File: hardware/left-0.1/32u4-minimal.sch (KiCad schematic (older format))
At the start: 15 parts, among them SW35 SW_Push, U2 ATmega32U4-AU, Y1 16MHz

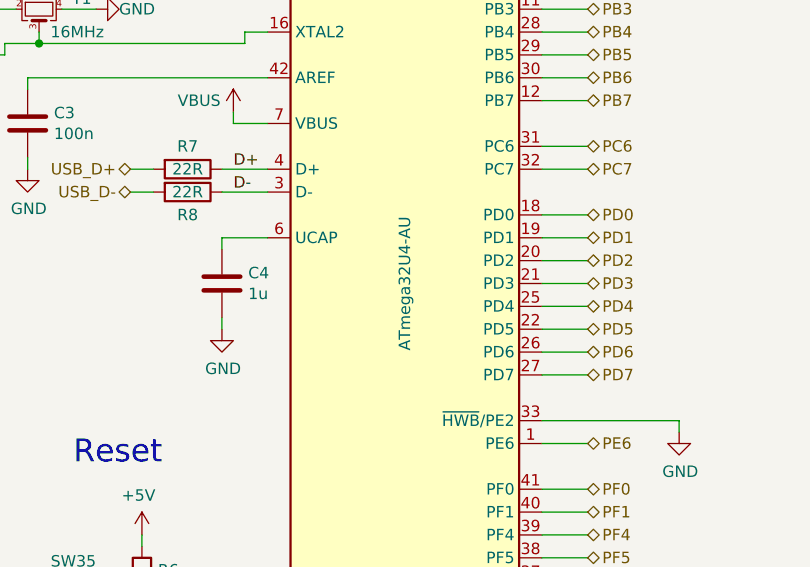
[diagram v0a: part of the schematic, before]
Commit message: first go at board outline done
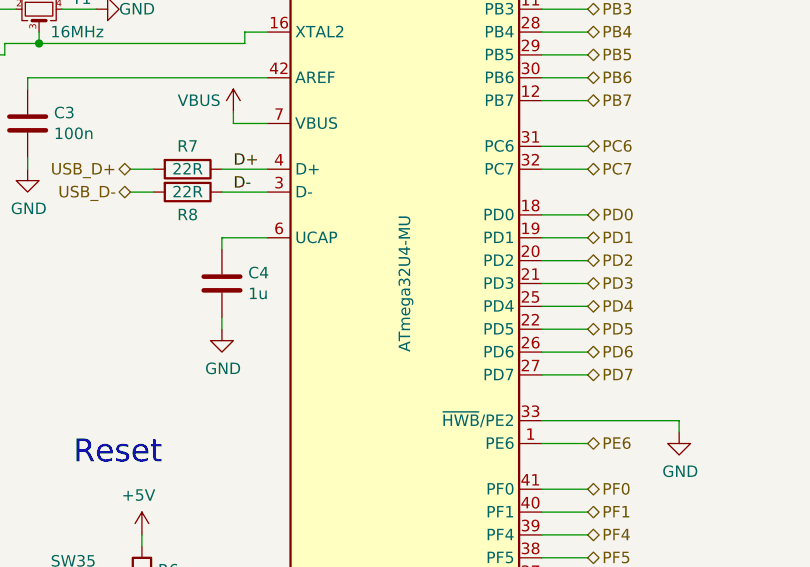
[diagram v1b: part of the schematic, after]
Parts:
- removed U2: ATmega32U4-AU, Package_QFP:TQFP-44_10x10mm_P0.8mm, symbol MCU_Microchip_ATmega:ATmega32U4-AU
- added U2: ATmega32U4-MU, Package_DFN_QFN:QFN-44-1EP_7x7mm_P0.5mm_EP5.2x5.2mm, symbol MCU_Microchip_ATmega:ATmega32U4-MU
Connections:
- net +5V: now also U2.14 (VCC), U2.24 (AVCC), U2.34 (VCC), U2.44 (AVCC)
- net D+: now also U2.4 (D+)
- net D-: now also U2.3 (D-)
- net GND: now also U2.15 (GND), U2.23 (GND), U2.33 (~HWB~/PE2), U2.35 (GND), U2.43 (GND), U2.45 (GND), U2.5 (UGND)
- net PB0: now also U2.8 (PB0)
- net PB1: now also U2.9 (PB1)
- net PB2: now also U2.10 (PB2)
- net PB3: now also U2.11 (PB3)
- net PB4: now also U2.28 (PB4)
- net PB5: now also U2.29 (PB5)
- net PB6: now also U2.30 (PB6)
- net PB7: now also U2.12 (PB7)
- net PC6: now also U2.31 (PC6)
- net PC7: now also U2.32 (PC7)
- net PD0: now also U2.18 (PD0)
- net PD1: now also U2.19 (PD1)
- net PD2: now also U2.20 (PD2)
- net PD3: now also U2.21 (PD3)
- net PD4: now also U2.25 (PD4)
- net PD5: now also U2.22 (PD5)
- net PD6: now also U2.26 (PD6)
- net PD7: now also U2.27 (PD7)
- net PE6: now also U2.1 (PE6)
- net PF0: now also U2.41 (PF0)
- net PF1: now also U2.40 (PF1)
- net PF4: now also U2.39 (PF4)
- net PF5: now also U2.38 (PF5)
- net PF6: now also U2.37 (PF6)
- net PF7: now also U2.36 (PF7)
- net VBUS: now also U2.2 (UVCC), U2.7 (VBUS)
- net nRST: now also U2.13 (~RESET)
- net at C1.1, Y1.1: now also U2.17 (XTAL1)
- net at C2.1, Y1.3: now also U2.16 (XTAL2)
- net at C4.1: now also U2.6 (UCAP)
- net at C3.1: now also U2.42 (AREF)
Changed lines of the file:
@@
 PF7
 $Comp
-L MCU_Microchip_ATmega:ATmega32U4-AU U2
-U 1 1 5F4370D6
+L MCU_Microchip_ATmega:ATmega32U4-MU U2
+U 1 1 5E24D58F
 P 3900 4400
 F 0 "U2" H 3450 6150 50  0000 C CNN
-F 1 "ATmega32U4-AU" V 3900 4400 50  0000 C CNN
-F 2 "Package_QFP:TQFP-44_10x10mm_P0.8mm" H 3900 4400 50  0001 C CIN
+F 1 "ATmega32U4-MU" V 3900 4400 50  0000 C CNN
+F 2 "Package_DFN_QFN:QFN-44-1EP_7x7mm_P0.5mm_EP5.2x5.2mm" H 3900 4400 50  0001 C CIN
 F 3 "http://ww1.microchip.com/downloads/en/DeviceDoc/Atmel-7766-8-bit-AVR-ATmega16U4-32U4_Datasheet.pdf" H 3900 4400 50  0001 C CNN
-F 4 "ATMEGA32U4-AURCT-ND" H 3900 4400 50  0001 C CNN "Digikey"
-F 5 "C44854" H 3900 4400 50  0001 C CNN "LCSC"
-F 6 "ATMEGA32U4-AU" H 3900 4400 50  0001 C CNN "MPN"
 	1    3900 4400
 	1    0    0    -1

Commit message: left all connected
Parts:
- added J3: AVR-ISP-6, josh-connectors:AVR_Programmer_SMD, symbol Connector:AVR-ISP-6
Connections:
- net +5V: now also J3.2 (VCC)
- net GND: now also J3.6 (GND)
- net PB1: now also J3.3 (SCK)
- net PB2: now also J3.4 (MOSI)
- net PB3: now also J3.1 (MISO)
- net nRST: now also J3.5 (~RST)
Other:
- note added: "Programming Header"
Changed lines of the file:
@@
 $Descr A4 11693 8268
 encoding utf-8
-Sheet 2 2
+Sheet 2 3
 Title ""
 Date ""
@@
 $Comp
 L MCU_Microchip_ATmega:ATmega32U4-MU U2
-U 1 1 5E24D58F
+U 1 1 5FB07BE0
 P 3900 4400
 F 0 "U2" H 3450 6150 50  0000 C CNN
@@
 	1    0    0    -1
 $EndComp
+$Comp
+L Connector:AVR-ISP-6 J3
+U 1 1 5E3F772B
+P 6450 5550
+F 0 "J3" H 6200 6000 50  0000 R CNN
+F 1 "AVR-ISP-6" H 6800 6000 50  0000 R CNN
+F 2 "josh-connectors:AVR_Programmer_SMD" V 6200 5600 50  0001 C CNN
+F 3 " ~" H 5175 5000 50  0001 C CNN
+	1    6450 5550
+	1    0    0    -1
+$EndComp
+Wire Wire Line
+	6350 5950 6350 6000
+$Comp
+L power:GND #PWR0209
+U 1 1 5E3FABE7
+P 6350 6000
+F 0 "#PWR0209" H 6350 5750 50  0001 C CNN
+F 1 "GND" H 6355 5827 50  0000 C CNN
+F 2 "" H 6350 6000 50  0001 C CNN
+F 3 "" H 6350 6000 50  0001 C CNN
+	1    6350 6000
+	1    0    0    -1
+$EndComp
+Wire Wire Line
+	6350 5050 6350 5000
+$Comp
+L power:+5V #PWR0210
+U 1 1 5E3FD90D
+P 6350 5000
+F 0 "#PWR0210" H 6350 4850 50  0001 C CNN
+F 1 "+5V" H 6365 5173 50  0000 C CNN
+F 2 "" H 6350 5000 50  0001 C CNN
+F 3 "" H 6350 5000 50  0001 C CNN
+	1    6350 5000
+	1    0    0    -1
+$EndComp
+Text Label 7150 5650 2    50   ~ 0
+nRST
+Wire Wire Line
+	7150 5650 6850 5650
+Text Notes 5800 4700 0    100  ~ 0
+Programming Header
+Text HLabel 7150 5350 2    50   BiDi ~ 0
+PB3
+Wire Wire Line
+	7150 5350 6850 5350
+Wire Wire Line
+	6850 5450 7150 5450
+Wire Wire Line
+	6850 5550 7150 5550
+Text HLabel 7150 5550 2    50   BiDi ~ 0
+PB1
+Text HLabel 7150 5450 2    50   BiDi ~ 0
+PB2
 $EndSCHEMATC

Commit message: layout looking nice, just graphics to go
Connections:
- no-connect marks 0 -> 3
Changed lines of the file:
@@
 Wire Wire Line
 	3300 4000 3100 4000
-$Comp
-L power:PWR_FLAG #FLG0104
-U 1 1 5E724506
-P 6850 7500
-F 0 "#FLG0104" H 6850 7575 50  0001 C CNN
-F 1 "PWR_FLAG" V 6850 7800 50  0000 C CNN
-F 2 "" H 6850 7500 50  0001 C CNN
-F 3 "~" H 6850 7500 50  0001 C CNN
-	1    6850 7500
-	1    0    0    -1
-$EndComp
-$Comp
-L power:GND #PWR0192
-U 1 1 5E727AD7
-P 6850 7550
-F 0 "#PWR0192" H 6850 7300 50  0001 C CNN
-F 1 "GND" H 6855 7377 50  0000 C CNN
-F 2 "" H 6850 7550 50  0001 C CNN
-F 3 "" H 6850 7550 50  0001 C CNN
-	1    6850 7550
-	1    0    0    -1
-$EndComp
-Wire Wire Line
-	6850 7550 6850 7500
 Text Label 3150 3900 0    50   ~ 0
 D+
@@
 Text HLabel 7150 5450 2    50   BiDi ~ 0
 PB2
+NoConn ~ 4500 3300
+NoConn ~ 4500 2900
+NoConn ~ 4500 4800
 $EndSCHEMATC

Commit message: updated components due to jlk change
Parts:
- J3: footprint josh-connectors:AVR_Programmer_SMD -> josh-connectors:AVR_PROG_2.54_SMT
- SW35: footprint josh-buttons-switches:BT_Small_2_Pin -> josh-buttons-switches:SW_Push_PTS820
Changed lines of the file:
@@
 F 0 "SW35" H 2450 6185 50  0000 C CNN
 F 1 "SW_Push" H 2450 6094 50  0000 C CNN
-F 2 "josh-buttons-switches:BT_Small_2_Pin" H 2450 6100 50  0001 C CNN
+F 2 "josh-buttons-switches:SW_Push_PTS820" H 2450 6100 50  0001 C CNN
 F 3 "~" H 2450 6100 50  0001 C CNN
 F 4 "401-1704-1-ND" H 2450 5900 50  0001 C CNN "Digikey"
@@
 F 0 "J3" H 6200 6000 50  0000 R CNN
 F 1 "AVR-ISP-6" H 6800 6000 50  0000 R CNN
-F 2 "josh-connectors:AVR_Programmer_SMD" V 6200 5600 50  0001 C CNN
+F 2 "josh-connectors:AVR_PROG_2.54_SMT" V 6200 5600 50  0001 C CNN
 F 3 " ~" H 5175 5000 50  0001 C CNN
 	1    6450 5550

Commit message: more layout
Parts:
- C1, C2: DigiKey (none) -> 1276-2228-1-ND; Digikey 1276-2228-1-ND -> (none)
- C3, C6, C7: DigiKey (none) -> 1276-1000-1-ND; Digikey 1276-1000-1-ND -> (none)
- C4, C5: DigiKey (none) -> 1276-1866-1-ND; Digikey 1276-1866-1-ND -> (none)
- D36: DigiKey (none) -> 732-4980-1-ND; Digikey 732-4980-1-ND -> (none)
- R5: DigiKey (none) -> CR0603-JW-222ELFCT-ND; Digikey CR0603-JW-222ELFCT-ND -> (none)
- R6: DigiKey (none) -> CR0603-JW-103ELFCT-ND; Digikey CR0603-JW-103ELFCT-ND -> (none)
- R7, R8: DigiKey (none) -> CR0603-JW-220ELFCT-ND; Digikey CR0603-JW-220ELFCT-ND -> (none)
- SW35: DigiKey (none) -> 401-1704-1-ND; Digikey 401-1704-1-ND -> (none)
- Y1: DigiKey (none) -> 535-9134-1-ND; Digikey 535-9134-1-ND -> (none)
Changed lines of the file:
@@
 F 2 "Capacitor_SMD:C_0603_1608Metric" H 4238 2100 50  0001 C CNN
 F 3 "~" H 4200 2250 50  0001 C CNN
-F 4 "1276-1000-1-ND" H 4200 2250 50  0001 C CNN "Digikey"
+F 4 "1276-1000-1-ND" H 4200 2250 50  0001 C CNN "DigiKey"
 F 5 "CL10B104KB8NNNC" H 4200 2250 50  0001 C CNN "MPN"
 	1    4200 2250
@@
 F 2 "Capacitor_SMD:C_0603_1608Metric" H 4238 1850 50  0001 C CNN
 F 3 "~" H 4200 2000 50  0001 C CNN
-F 4 "1276-1000-1-ND" H 4200 2000 50  0001 C CNN "Digikey"
+F 4 "1276-1000-1-ND" H 4200 2000 50  0001 C CNN "DigiKey"
 F 5 "CL10B104KB8NNNC" H 4200 2000 50  0001 C CNN "MPN"
 	1    4200 2000
@@
 F 2 "Capacitor_SMD:C_0603_1608Metric" H 4238 1600 50  0001 C CNN
 F 3 "~" H 4200 1750 50  0001 C CNN
-F 4 "1276-1866-1-ND " H 4200 1750 50  0001 C CNN "Digikey"
+F 4 "1276-1866-1-ND " H 4200 1750 50  0001 C CNN "DigiKey"
 F 5 "CL10A105MP8NNNC " H 4200 1750 50  0001 C CNN "MPN"
 	1    4200 1750
@@
 F 2 "Capacitor_SMD:C_0603_1608Metric" H 1988 2850 50  0001 C CNN
 F 3 "~" H 1950 3000 50  0001 C CNN
-F 4 "1276-2228-1-ND " H 1950 3000 50  0001 C CNN "Digikey"
+F 4 "1276-2228-1-ND " H 1950 3000 50  0001 C CNN "DigiKey"
 F 5 "CL10C220JB8NFNC " H 1950 3000 50  0001 C CNN "MPN"
 	1    1950 3000
@@
 F 2 "Capacitor_SMD:C_0603_1608Metric" H 1988 3250 50  0001 C CNN
 F 3 "~" H 1950 3400 50  0001 C CNN
-F 4 "1276-2228-1-ND " H 1950 3400 50  0001 C CNN "Digikey"
+F 4 "1276-2228-1-ND " H 1950 3400 50  0001 C CNN "DigiKey"
 F 5 "CL10C220JB8NFNC " H 1950 3400 50  0001 C CNN "MPN"
 	1    1950 3400
@@
 F 2 "josh-oscillators:Crystal_SMD_3225-4Pin_3.2x2.5mm" H 2300 3200 50  0001 C CNN
 F 3 "~" H 2300 3200 50  0001 C CNN
-F 4 "535-9134-1-ND" H 2300 3200 50  0001 C CNN "Digikey"
+F 4 "535-9134-1-ND" H 2300 3200 50  0001 C CNN "DigiKey"
 F 5 "C179641" H 2300 3200 50  0001 C CNN "LCSC"
 F 6 "ABM8-16.000MHZ-B2-T" H 2300 3200 50  0001 C CNN "MPN"
@@
 F 2 "Capacitor_SMD:C_0603_1608Metric" H 3138 4250 50  0001 C CNN
 F 3 "~" H 3100 4400 50  0001 C CNN
-F 4 "1276-1866-1-ND " H 3100 4400 50  0001 C CNN "Digikey"
+F 4 "1276-1866-1-ND " H 3100 4400 50  0001 C CNN "DigiKey"
 F 5 "CL10A105MP8NNNC " H 3100 4400 50  0001 C CNN "MPN"
 	1    3100 4400
@@
 F 2 "Capacitor_SMD:C_0603_1608Metric" H 2288 3550 50  0001 C CNN
 F 3 "~" H 2250 3700 50  0001 C CNN
-F 4 "1276-1000-1-ND" H 2250 3700 50  0001 C CNN "Digikey"
+F 4 "1276-1000-1-ND" H 2250 3700 50  0001 C CNN "DigiKey"
 F 5 "CL10B104KB8NNNC" H 2250 3700 50  0001 C CNN "MPN"
 	1    2250 3700
@@
 F 2 "josh-buttons-switches:SW_Push_PTS820" H 2450 6100 50  0001 C CNN
 F 3 "~" H 2450 6100 50  0001 C CNN
-F 4 "401-1704-1-ND" H 2450 5900 50  0001 C CNN "Digikey"
+F 4 "401-1704-1-ND" H 2450 5900 50  0001 C CNN "DigiKey"
 F 5 "C354946" H 2450 5900 50  0001 C CNN "LCSC"
 F 6 "KSR223GLFG" H 2450 5900 50  0001 C CNN "MPN"
@@
 F 2 "Resistor_SMD:R_0603_1608Metric" V 2680 5700 50  0001 C CNN
 F 3 "~" H 2750 5700 50  0001 C CNN
-F 4 "CR0603-JW-103ELFCT-ND  " H 2750 5700 50  0001 C CNN "Digikey"
+F 4 "CR0603-JW-103ELFCT-ND  " H 2750 5700 50  0001 C CNN "DigiKey"
 F 5 "CR0603-JW-103ELF " H 2750 5700 50  0001 C CNN "MPN"
 	1    2750 5700
@@
 F 2 "LED_SMD:LED_0603_1608Metric_Castellated" H 1800 5750 50  0001 C CNN
 F 3 "~" H 1800 5750 50  0001 C CNN
-F 4 "732-4980-1-ND  " H 1800 5750 50  0001 C CNN "Digikey"
+F 4 "732-4980-1-ND  " H 1800 5750 50  0001 C CNN "DigiKey"
 F 5 "150060VS75000" H 1800 5750 50  0001 C CNN "MPN"
 	1    1800 5750
@@
 F 2 "Resistor_SMD:R_0603_1608Metric" V 1730 5400 50  0001 C CNN
 F 3 "~" H 1800 5400 50  0001 C CNN
-F 4 "CR0603-JW-222ELFCT-ND  " H 1800 5400 50  0001 C CNN "Digikey"
+F 4 "CR0603-JW-222ELFCT-ND  " H 1800 5400 50  0001 C CNN "DigiKey"
 F 5 "CR0603-JW-222ELF " H 1800 5400 50  0001 C CNN "MPN"
 	1    1800 5400
@@
 F 2 "Resistor_SMD:R_0603_1608Metric" V 2880 3900 50  0001 C CNN
 F 3 "~" H 2950 3900 50  0001 C CNN
-F 4 "CR0603-JW-220ELFCT-ND  " H 2950 3900 50  0001 C CNN "Digikey"
+F 4 "CR0603-JW-220ELFCT-ND  " H 2950 3900 50  0001 C CNN "DigiKey"
 F 5 "CR0603-JW-220ELF " H 2950 3900 50  0001 C CNN "MPN"
 	1    2950 3900
@@
 F 2 "Resistor_SMD:R_0603_1608Metric" V 2880 4000 50  0001 C CNN
 F 3 "~" H 2950 4000 50  0001 C CNN
-F 4 "CR0603-JW-220ELFCT-ND  " H 2950 4000 50  0001 C CNN "Digikey"
+F 4 "CR0603-JW-220ELFCT-ND  " H 2950 4000 50  0001 C CNN "DigiKey"
 F 5 "CR0603-JW-220ELF " H 2950 4000 50  0001 C CNN "MPN"
 	1    2950 4000
